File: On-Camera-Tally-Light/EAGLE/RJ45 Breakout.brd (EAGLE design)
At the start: 32.9 x 31.7 mm, 6 parts, among them J1 MAGJACK

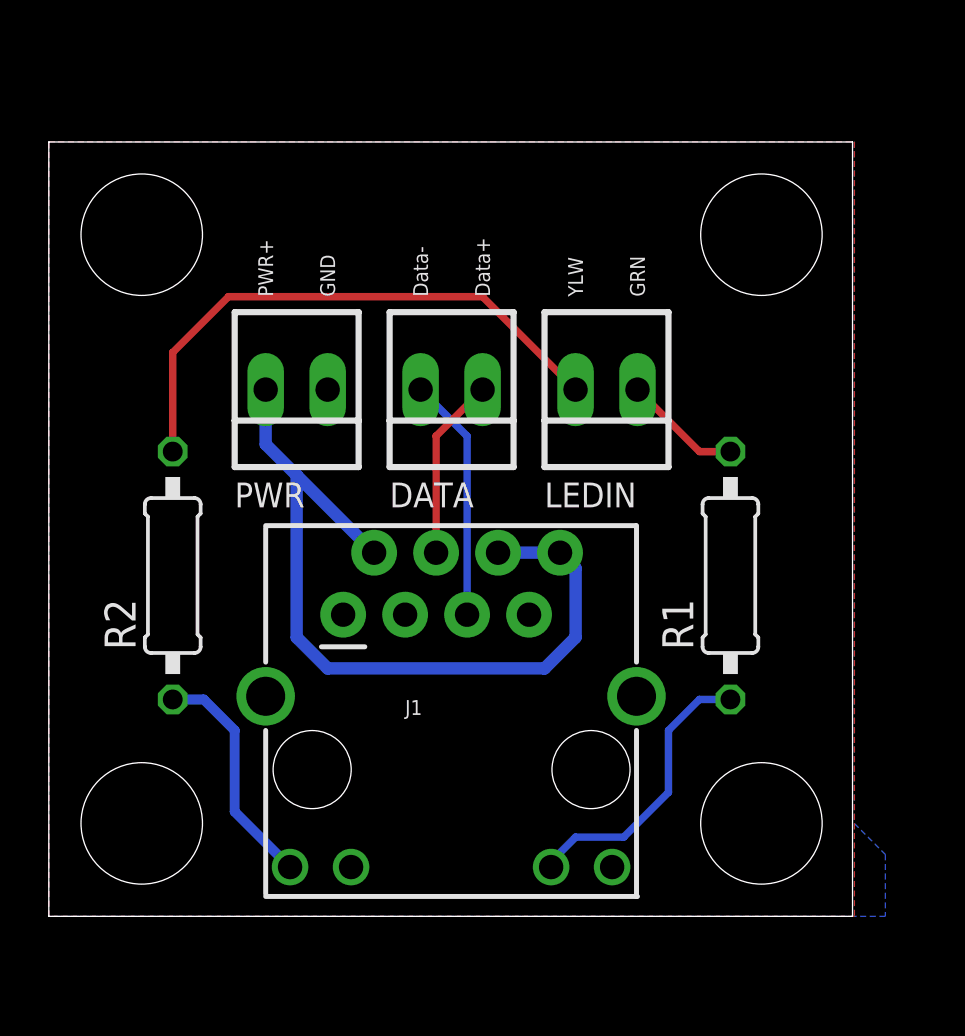
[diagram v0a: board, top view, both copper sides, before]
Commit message: Standardize RS485 pinouts, update RJ45 pinouts.
Fix pin assignments for the RS485 interconnects to standardize on pin1 = data-.
Update the RJ45 breakouts to be mostly pin compatible with DMX over ethernet wiring standard (using pin 5/6 for V+)
Create an XLR RS485 breakout option for wiring cameras together using 3pin DMX cables
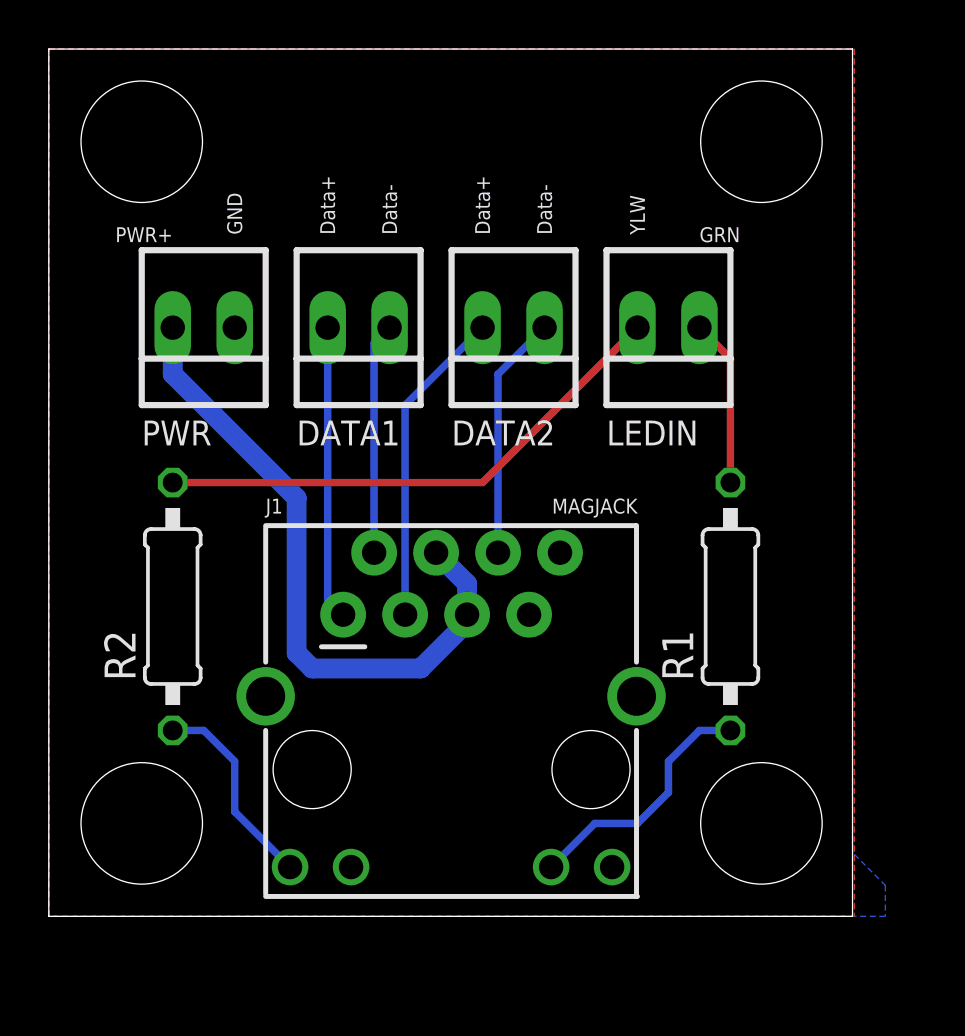
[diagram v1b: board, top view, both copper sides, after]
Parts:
- removed DATA: 22-23-2021, con-molex:22-23-2021
- added DATA1, DATA2: 22-23-2021, con-molex:22-23-2021
- moved PWR 4.58 mm to (6.35, 24.1)
- moved LEDIN 3.59 mm to (25.4, 24.1)
- moved R1 1.27 mm to (27.9, 12.7)
- moved R2 1.27 mm to (5.08, 12.7)
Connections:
- removed net DATA+: DATA.1, J1.4
- removed net DATA-: DATA.2, J1.5
- new net DATA1+: DATA1.2, J1.1
- new net DATA1-: DATA1.1, J1.2
- new net DATA2+: DATA2.2, J1.3
- new net DATA2-: DATA2.1, J1.6
- net GND: now also J1.8; no longer J1.1, J1.3
- net PWR: now also J1.4, J1.5; no longer J1.2, J1.6, J1.8
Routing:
- net DATA2+: track 0.00 -> 13.1 mm
- net DATA1+: track 0.00 -> 12.0 mm
- net DATA2-: track 0.00 -> 10.0 mm
- net DATA-: track 10.0 -> 0.00 mm
- net DATA1-: track 0.00 -> 9.49 mm
- net DATA+: track 7.47 -> 0.00 mm
- net PWR: track 33.9 -> 26.8 mm
- net GRN: track 4.86 -> 6.88 mm
- net YLW: track 23.1 -> 21.7 mm
- net GRNIN: track 11.8 -> 10.4 mm
- net YLWIN: track 9.61 -> 8.34 mm
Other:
- board size 32.9 x 31.7 mm -> 32.9 x 35.5 mm

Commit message: Update RJ45 boards to use RJHSE Amphenol jacks
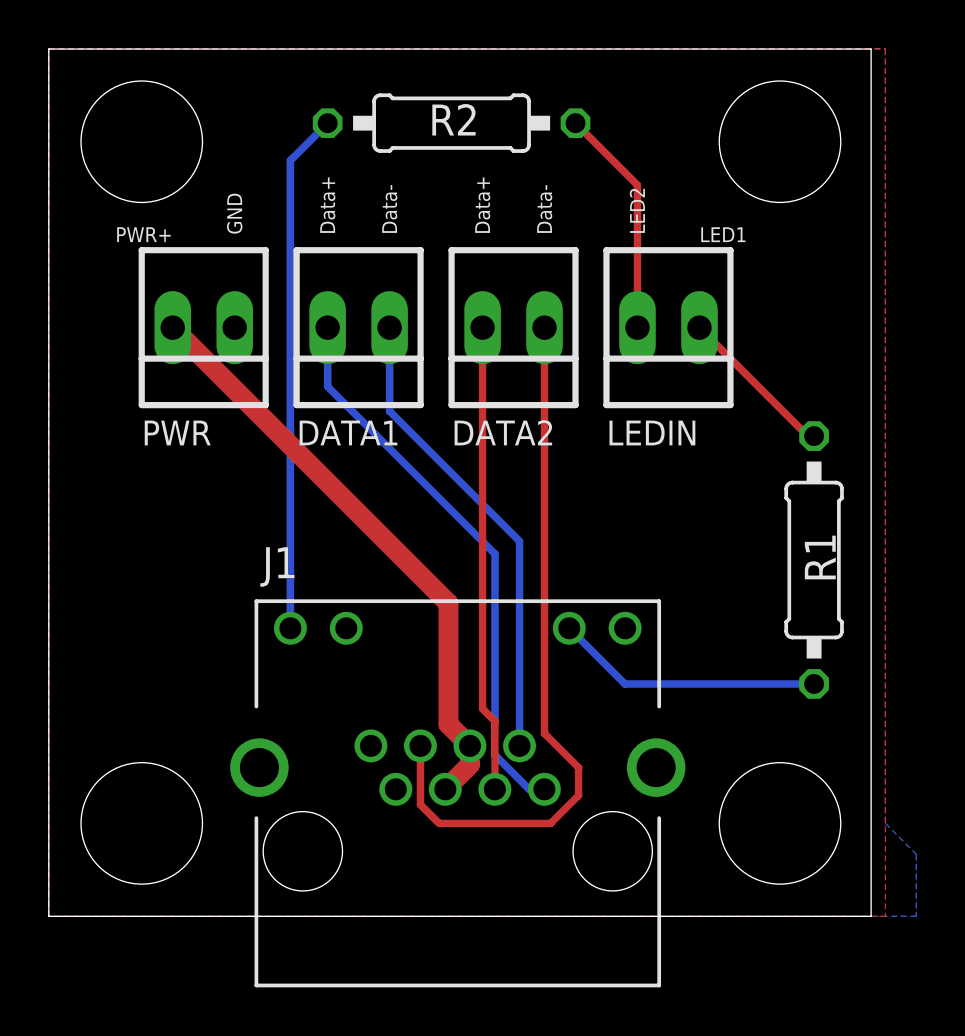
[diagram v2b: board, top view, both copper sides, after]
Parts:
- J1: value MAGJACK -> RJHSE-5381; device SparkFun-Connectors:MAGJACK -> RJHSE-5381:AMPHENOL_RJHSE-5381
- moved R2 22.9 mm to (16.5, 32.5), turned to 180 degrees
- moved J1 11.0 mm to (16.8, 2.67)
- moved R1 3.92 mm to (31.4, 14.6), turned to 270 degrees
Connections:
- net PWR renamed VCC
- removed net GRN: LEDIN.1, R1.2
- removed net GRNIN: J1.11, R1.1
- removed net YLW: LEDIN.2, R2.2
- removed net YLWIN: J1.9, R2.1
- new net LED1: J1.10, R1.2
- new net LED1IN: LEDIN.1, R1.1
- new net LED2: J1.12, R2.2
- new net LED2IN: LEDIN.2, R2.1
- net GND: now also J1.11, J1.9, J1.S1, J1.S2; no longer J1.10, J1.12, J1.M1, J1.M2
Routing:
- net YLW: track 21.7 -> 0.00 mm
- net LED2: track 0.00 -> 21.3 mm
- net DATA2-: track 10.0 -> 29.4 mm
- net LED1: track 0.00 -> 11.0 mm
- net DATA1+: track 12.0 -> 23.0 mm
- net GRNIN: track 10.4 -> 0.00 mm
- net DATA1-: track 9.49 -> 19.3 mm
- net LED2IN: track 0.00 -> 9.43 mm
- net YLWIN: track 8.34 -> 0.00 mm
- net GRN: track 6.88 -> 0.00 mm
- net LED1IN: track 0.00 -> 6.54 mm
- net DATA2+: track 13.1 -> 19.1 mm
- net VCC: track 26.8 -> 24.4 mm
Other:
- board size 32.9 x 35.5 mm -> 33.7 x 35.5 mm
- board text added: "LED1"
- board text added: "LED2"
- board text added: "RS485 + Power Breakout"
- board text removed: "GRN"
- board text removed: "RS485 + 24V Power Breakout w/ status LEDs"
- board text removed: "YLW"
